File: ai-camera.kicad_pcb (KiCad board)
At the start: 4 copper layers, 70 x 70 mm, 177 parts, among them J1 Conn-01x02_P2mm_S2B-PH-K-S_Ho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, J2 USB_B_Micro_10118194-0001LF, J3 DBG, J4 Conn-02x10_P2.54mm_B-2100S20P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, J5 Conn-01x02_P1.25mm_10114829-1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, J6 Conn_01x24_FFC_0.5mm_hirose_F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, J7 Conn_01x24_FFC_0.5mm_hirose_F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, Q1 AO3401A, Q2 AO3400A, Q3 AO3400A, Q4 AO3401A, Q5 AO3400A, Q6 AO3401A, Q7 AO3400A, SW1 SW_PB_TS-1187A-B-A-B, SW2 SW_PB_TS-1187A-B-A-B, SW3 SW_PB_TS-1187A-B-A-B, SW4 SW_PB_TS-1187A-B-A-B, U1 SRV05-4, U10 AP1511B, U11 ESP32-S3-WROOM-1-N16R8, U12 MT9284-28J, U2 TP4057-42-SOT26-R, U3 PCF8563T/5,518, U4 XC6206-2.8V, U5 PIR_BS612, U6 SY8089AAAC, U7 SOT-23-6_SN74LVC1G373DBVR_TI, U8 XC6206-2.8V, U9 RT9166-12GVL, Y1 32.768kHz_Q13FC1350000400

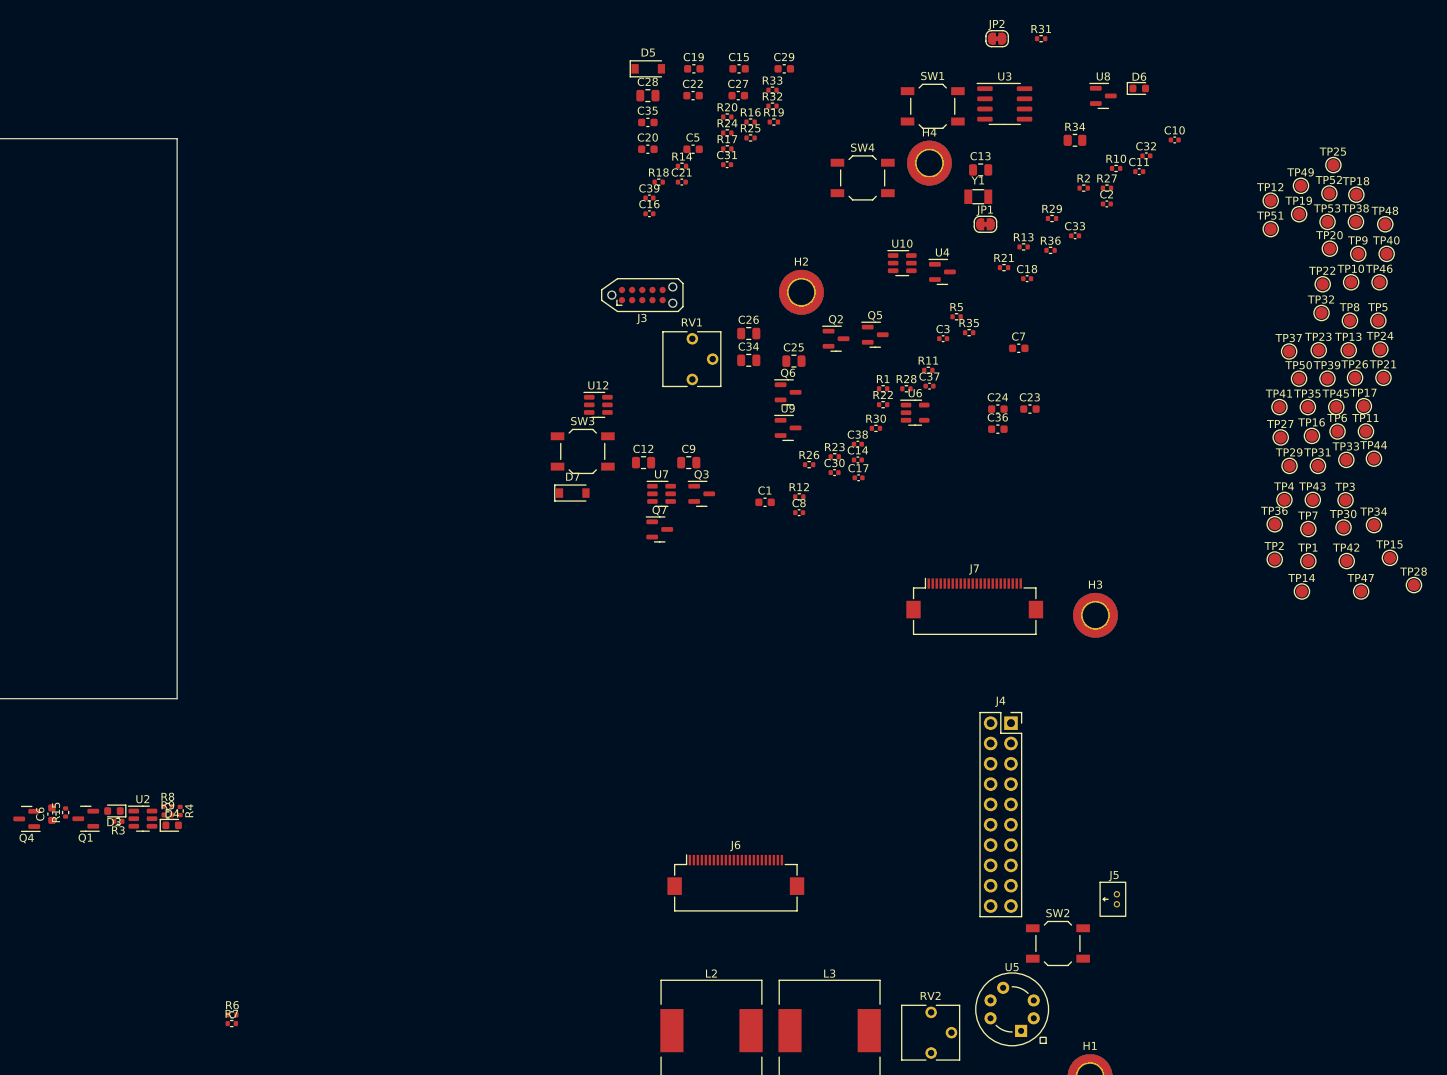
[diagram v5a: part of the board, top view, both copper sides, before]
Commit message: ai camera review 14: add aliases to CAM.SDA/SCL to confuse schematics less
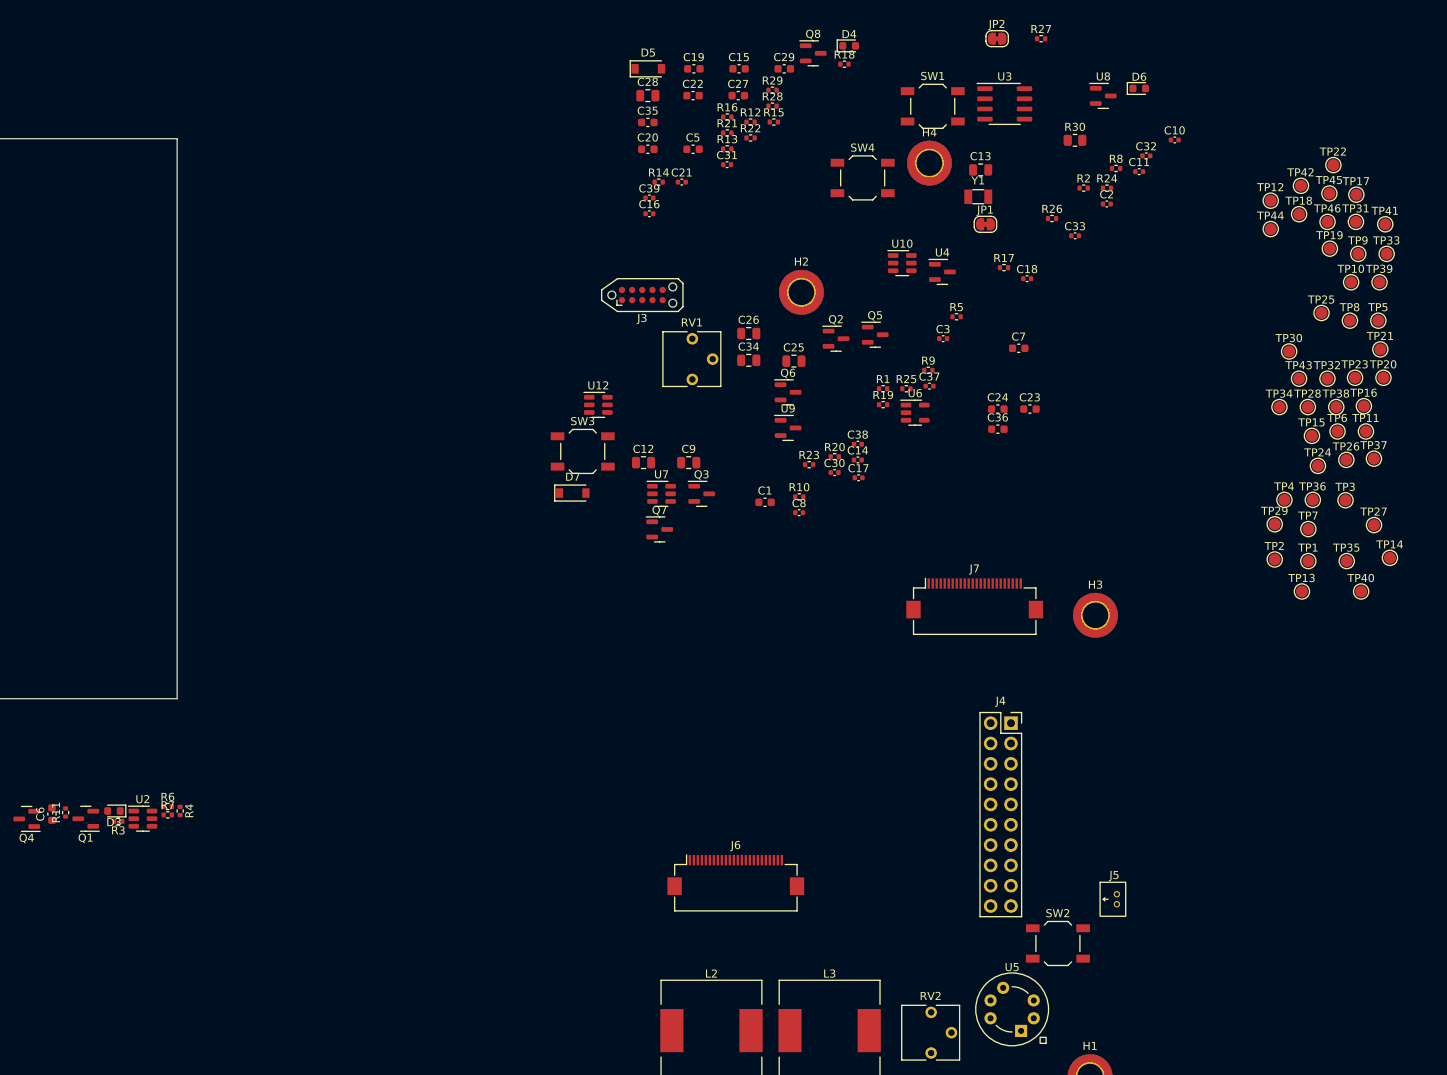
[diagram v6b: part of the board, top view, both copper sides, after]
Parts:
- removed the R13 at (270.8, 58.5)
- removed the R14 at (228.1, 48.4)
- removed the R30 at (252.3, 81.2)
- removed R35, R36: 10k_0402_0402WGF1002TCE, Resistor_SMD:R_0402_1005Metric
- removed the R6 at (171.9, 154.5)
- removed the R7 at (171.8, 155.6)
- removed the TP13 at (311.4, 71.5)
- removed the TP22 at (308.2, 63.2)
- removed the TP23 at (307.7, 71.5)
- removed the TP27 at (302.9, 82.3)
- removed the TP28 at (319.6, 100.8)
- removed the TP29 at (304.1, 85.9)
- removed the TP30 at (310.8, 93.6)
- added Q8: AO3400A, Package_TO_SOT_SMD:SOT-23, F.Cu at (244.5, 34.3)
- added R18: 215k_0402_0402WGD2153TCE, Resistor_SMD:R_0402_1005Metric, F.Cu at (248.4, 35.7)
- D4: value 0603_RED_KT-0603R -> 0603_GREEN_19-217/GHC-YR1S2/3T
- moved D4 129.0 mm to (249.0, 33.4)
- renumbered R12 to R10, R15 to R11, R16 to R12, R17 to R13, R18 to R14, R19 to R15, R20 to R16, R21 to R17, R22 to R19, R23 to R20, R24 to R21, R25 to R22, R26 to R23, R27 to R24, R28 to R25, R29 to R26, R31 to R27, R32 to R28, R33 to R29, R34 to R30, R8 to R6, R9 to R7, R10 to R8, R11 to R9, TP14 to TP13, TP15 to TP14, TP16 to TP15, TP17 to TP16, TP18 to TP17, TP19 to TP18, TP20 to TP19, TP21 to TP20, TP24 to TP21, TP25 to TP22, TP26 to TP23, TP31 to TP24, TP32 to TP25, TP33 to TP26, TP34 to TP27, TP35 to TP28, TP36 to TP29, TP37 to TP30, TP38 to TP31, TP39 to TP32, TP40 to TP33, TP41 to TP34, TP42 to TP35, TP43 to TP36, TP44 to TP37, TP45 to TP38, TP46 to TP39, TP47 to TP40, TP48 to TP41, TP49 to TP42, TP50 to TP43, TP51 to TP44, TP52 to TP45, TP53 to TP46
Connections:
- J4 pad 11: /SDA -> /CAM.SDA
- J4 pad 13: /SCL -> /CAM.SCL
- J4 pad 18: GND -> /IO2
- J7 pad 2: /SDA -> /CAM.SDA
- J7 pad 3: /SCL -> /CAM.SCL
- Q2 pad 2: /SCL -> /CAM.SCL
- Q3 pad 2: /SDA -> /CAM.SDA
- U11 pad 24: /SDA -> /PIR_OUT
- U11 pad 25: /SCL -> /IRCUT_CTRL
- U11 pad 38: /DBG_DETECT -> /IO2

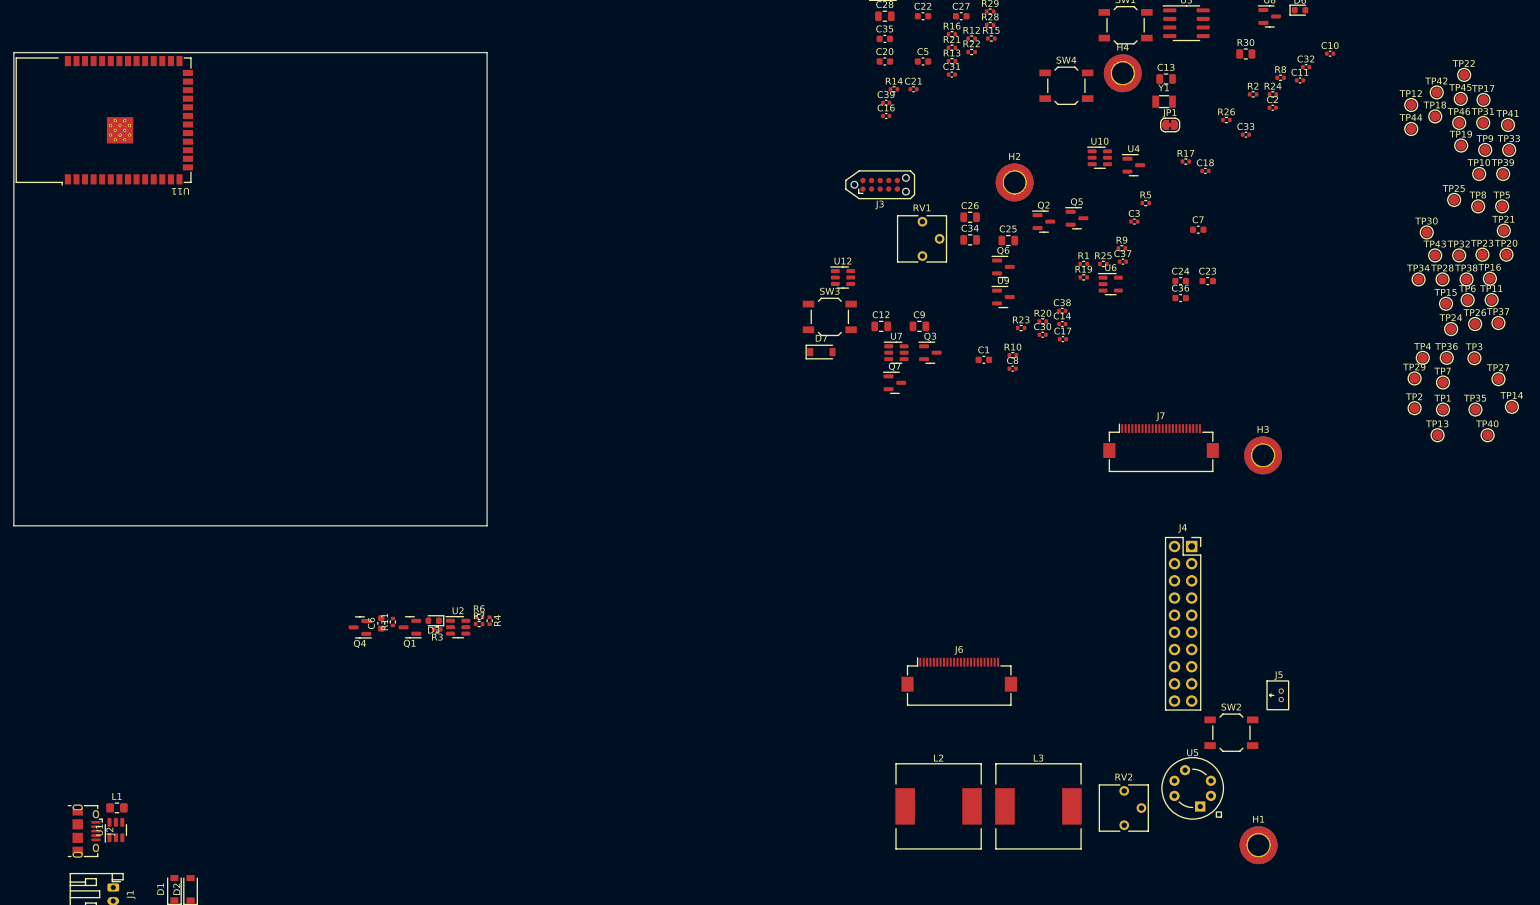
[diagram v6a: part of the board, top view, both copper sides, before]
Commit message: ai camera layout: MCU and camera placement
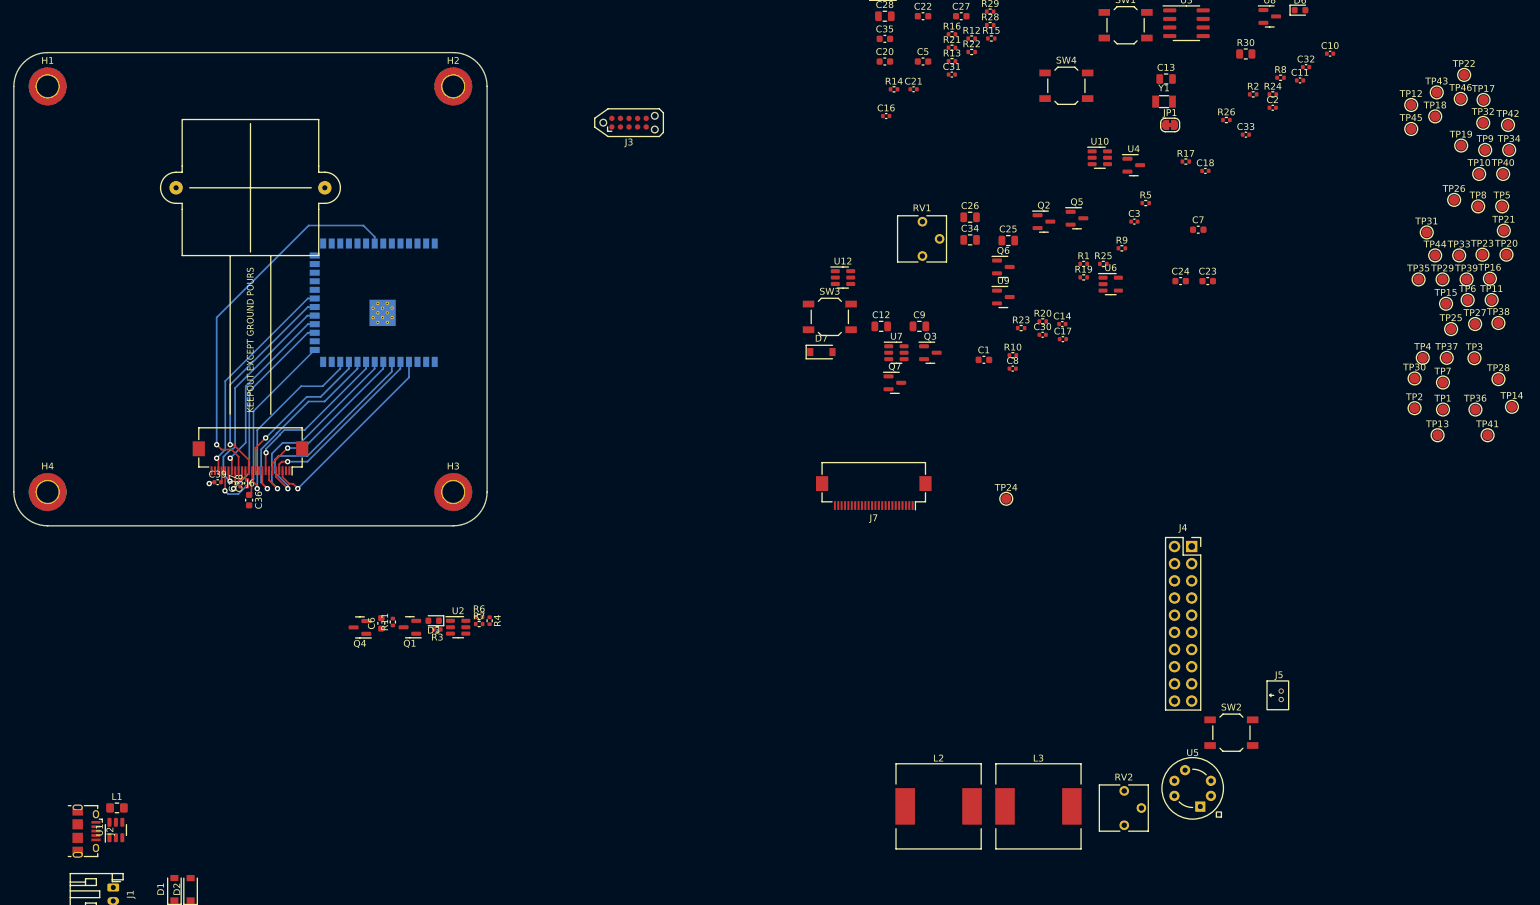
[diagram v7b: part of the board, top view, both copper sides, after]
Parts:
- removed the TP46 at (308.8, 55.4)
- added REF**: ircut_filter_M12_30mm_noname, 00-kiml-optical:ircut_filter_M12_30mm_noname, F.Cu at (130.0, 65.0)
- added TP24: TP, TestPoint:TestPoint_Pad_D1.5mm, F.Cu at (241.8, 111.0)
- U11: moved to B.Cu
- moved H1 211.4 mm to (100.0, 50.0)
- moved H4 170.7 mm to (100.0, 110.0)
- moved C36 141.0 mm to (129.8, 111.2), turned to -90 degrees
- moved C37 134.6 mm to (128.5, 108.7), turned to 90 degrees
- moved C38 123.3 mm to (129.5, 108.7), turned to 90 degrees
- moved H3 119.9 mm to (160.0, 110.0)
- moved C39 113.7 mm to (125.2, 108.5)
- moved J6 109.6 mm to (130.0, 105.0), turned to 180 degrees
- moved H2 84.2 mm to (160.0, 50.0)
- moved U11 51.4 mm to (152.0, 82.0)
- moved J7 43.2 mm to (222.2, 110.2), turned to 180 degrees
- moved J3 38.3 mm to (186.0, 55.4)
- renumbered TP24 to TP25, TP25 to TP26, TP26 to TP27, TP27 to TP28, TP28 to TP29, TP29 to TP30, TP30 to TP31, TP31 to TP32, TP32 to TP33, TP33 to TP34, TP34 to TP35, TP35 to TP36, TP36 to TP37, TP37 to TP38, TP38 to TP39, TP39 to TP40, TP40 to TP41, TP41 to TP42, TP42 to TP43, TP43 to TP44, TP44 to TP45, TP45 to TP46
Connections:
- J3 pad 2: unconnected-(J3-Pad2) -> +3V3
- J4 pad 11: /CAM.SDA -> /CAM.SCL
- J4 pad 13: /CAM.SCL -> /CAM.SDA
- J7 pad 2: /CAM.SDA -> /CAM.SCL
- J7 pad 3: /CAM.SCL -> /CAM.SDA
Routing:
- net /CAM.HREF: track 0.00 -> 55.6 mm, vias 0 -> 1
- net /CAM.RST: track 0.00 -> 32.9 mm, vias 0 -> 1
- net /CAM.D5: track 0.00 -> 32.6 mm, vias 0 -> 1
- net /CAM.SDA: track 0.00 -> 32.2 mm, vias 0 -> 1
- net /CAM.D9: track 0.00 -> 31.4 mm, vias 0 -> 1
- net /CAM.PWDN: track 0.00 -> 31.4 mm, vias 0 -> 1
- net /CAM.SCL: track 0.00 -> 31.2 mm, vias 0 -> 1
- net /CAM.D6: track 0.00 -> 30.1 mm, vias 0 -> 1
- net /CAM.D4: track 0.00 -> 29.5 mm, vias 0 -> 1
- net /CAM.D7: track 0.00 -> 29.4 mm, vias 0 -> 1
- net /CAM.MCLK: track 0.00 -> 28.7 mm, vias 0 -> 1
- net /CAM.VSYNC: track 0.00 -> 27.5 mm, vias 0 -> 1
- net /CAM.D3: track 0.00 -> 25.7 mm, vias 0 -> 1
- net /CAM.D2: track 0.00 -> 24.3 mm, vias 0 -> 1
- net /CAM.PCLK: track 0.00 -> 24.0 mm, vias 0 -> 1
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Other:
- outline, holes or cut-outs redrawn
